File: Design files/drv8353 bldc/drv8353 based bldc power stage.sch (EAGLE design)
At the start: 110 parts, among them IC1 DRV8350RSRGZT, J3 2X6 FEMALE, J4 B06B-HCMKK

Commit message: started layout of power stage
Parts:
- removed BB2: (no value), busbar:TE3/2
- removed C1: 0.1uF, resistor:C-EUC0603K
- removed C10, C11, C12: 2200pF, rcl:C-EUC0603K
- removed C13: 1 uF, rcl:C-EUC1206K
- removed C14: .1 uF, resistor:C-EUC0805K
- removed C15, C16, C17: 1 uF, rcl:C-EUC0603K
- removed C18: .01uF, rcl:C-EUC0603K
- removed C19: 3600pF, rcl:C-EUC0603K
- removed C20: 2.2uF, rcl:C-EUC0805K
- removed C21: .047 uF, rcl:C-EUC0805K
- removed C22: 1 uF, resistor:C-EUC0603K
- removed C25: .1 uF, rcl:C-EUC0805K
- removed C26: 10 uF, rcl:C-EUC2220K
- removed C27: 1 uF, rcl:C-EUC0805K
- removed C28: .01 uF, rcl:C-EUC0603K
- removed C29: 4.7 uF, rcl:C-EUC1210K
- removed D4: DFLS1200, REV BLDC:DFLS1200
- removed IC1: DRV8350RSRGZT, REV BLDC:DRV8350RSRGZT
- removed J3: 2X6 FEMALE, pinhead:PINHD-2X6
- removed J4: B06B-HCMKK, SamacSys_Parts:B06B-HCMKK
- removed JP1: (no value), pinhead:PINHD-1X2
- removed L3: 330 uH, REV BLDC:74404084331
- removed LDO: LP2992IM5-5.0_NOPB, SamacSys_Parts:LP2992IM5-5.0_NOPB
- removed LED1: (no value), eagle-ltspice:LED_ESML0603
- removed R1, R_FB1: 10k, rcl:R-US_R0603
- removed R10, R11, R12: 56, rcl:R-US_R0603
- removed R13: 107k, rcl:R-US_R0603
- removed R14: 274k, rcl:R-US_R0603
- removed R17: 2.61, rcl:R-US_R0603
- removed R2: 330, rcl:R-US_R0603
- removed R20: 1k, rcl:R-US_R0603
- removed R3: 5K, resistor:R-US_R0603
- removed R4, R5: 0, resistor:R-US_R0603
- removed R_FB2: 2.61k, rcl:R-US_R0603
- removed S1: RDT1034, switch:RDT1034
- removed SV1: (no value), pinhead:PINHD-1X3
- removed TP10, TP11, TP12, TP15, TP19, TP32, TP33, TP34, TP36, TP40, TP5, TP6, TP7, TP8, TP9: TPB1,27, testpad:TPB1,27
- removed TVS_DIODE: TPD4S010DQAR, REV BLDC:TPD4S010DQAR
- removed U$1: ZENER, REV BLDC:ZENER
- removed U$2: BOOSTER_DOCK, REV BLDC:BOOSTER_DOCK
- added U$11, U$12, U$13, U$15, U$4, U$5: ZENER_PACK, REV BLDC:ZENER_PACK
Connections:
- removed net 3V3: J4.2, JP1.2, R1.2, R2.2, R20.2, U$2.1
- removed net AGND: IC1.AGND, R4.1, TP40.TP
- removed net BST: C18.2, IC1.BST
- removed net CPH: C21.2, IC1.CPH
- removed net CPL: C21.1, IC1.CPL
- removed net CS: IC1.NSCS, J3.10, U$2.19
- removed net DRV_VM: C25.1, C26.1, IC1.VM, SV1.2, TP15.TP
- removed net ENABLE: IC1.ENABLE, R3.1, S1.B, U$2.11
- removed net FB: C19.2, IC1.FB, R_FB1.1, R_FB2.2
- removed net HALL_A: J4.3, U$2.34
- removed net HALL_B: J4.4, U$2.33
- removed net HALL_C: J4.5, U$2.32
- removed net INHA: IC1.INHA, J3.11, U$2.40
- removed net INHB: IC1.INHB, J3.7, U$2.38
- removed net INHC: IC1.INHC, J3.6, U$2.36
- removed net INLA: IC1.INLA, J3.9, U$2.39
- removed net INLB: IC1.INLB, J3.8, U$2.37
- removed net INLC: IC1.INLC, J3.4, U$2.35
- removed net ISENA: C10.1, R10.1, U$2.27
- removed net ISENB: C11.1, R11.1, U$2.28
- removed net ISENC: C12.1, R12.1, U$2.29
- removed net MISO: IC1.SDO, J3.1, R20.1, U$2.14
- removed net MOSI: IC1.SDI, J3.3, U$2.15
- removed net N$1: C15.2, IC1.DVDD
- removed net N$13: C28.2, LDO.BYPASS
- removed net N$14: C20.1, R17.1
- removed net N$16: LED1.A, R2.1
- removed net N$2: C29.2, JP1.1, LDO.VOUT
- removed net N$20: C1.1, R3.2
- removed net NFAULT: IC1.NFAULT, LED1.C, R1.1, U$2.12
- removed net PGND: R5.1, TP19.TP, U$2.2
- removed net RCL: IC1.RCL, R13.2
- removed net RT/SD: IC1.RT/SD, R14.2
- removed net SCLK: IC1.SCLK, J3.5, U$2.7
- removed net SW: C18.1, D4.LINE, IC1.SW, L3.2
- removed net VBUCK: C19.1, C20.2, C27.2, L3.1, LDO.IN, LDO.ON/!OFF, R_FB1.2, SV1.1, U$1.LINE
- removed net VCC: C17.2, IC1.VCC
- removed net VCP: C22.2, IC1.VCP
- removed net VGLS: C16.2, IC1.VGLS
- net APHASE: now also U$5.END2; no longer IC1.SHA, TP32.TP
- net BPHASE: now also U$11.END2; no longer IC1.SHB, TP6.TP
- net CPHASE: now also U$13.END2; no longer IC1.SHC, TP12.TP
- net GHA: now also U$5.END1; no longer IC1.GHA, TP36.TP
- net GHB: now also U$11.END1; no longer IC1.GHB, TP8.TP
- net GHC: now also U$13.END1; no longer IC1.GHC, TP9.TP
- net GLA: now also U$4.END1; no longer IC1.GLA, TP33.TP
- net GLB: now also U$12.END1; no longer IC1.GLB, TP7.TP
- net GLC: now also U$15.END1; no longer IC1.GLC, TP11.TP
- net GND: no longer BB2.P@1, BB2.P@2, C1.2, C10.2, C11.2, C12.2, C13.2, C14.1, C15.1, C16.1, C17.1, C25.2, C26.2, C27.1, C28.1, C29.1, D4.GND, IC1.DGND, IC1.GND_1, IC1.GND_2, J3.12, J3.2, J4.6, LDO.GND, R13.1, R17.2, R4.2, R5.2, R_FB2.1, S1.A, S1.A1, TVS_DIODE.AGND, TVS_DIODE.GND, U$1.A, U$2.20, U$2.22
- net SLA: now also U$4.END2; no longer IC1.SLA, TP34.TP
- net SLB: now also U$12.END2; no longer IC1.SLB, TP5.TP
- net SLC: now also U$15.END2; no longer IC1.SLC, TP10.TP
- net SOA: no longer R10.2
- net SOB: no longer R11.2
- net SOC: no longer R12.2
- net VDRAIN: no longer C13.1, C14.2, C22.1, IC1.VDRAIN, IC1.VIN, R14.1, SV1.3
- net VSENA: no longer TVS_DIODE.D2+, TVS_DIODE.NC2, U$2.30
- net VSENB: no longer TVS_DIODE.D1-, TVS_DIODE.NC3, U$2.25
- net VSENC: no longer TVS_DIODE.D1+, TVS_DIODE.NC4, U$2.26
- net VSENVM: no longer TVS_DIODE.D2-, TVS_DIODE.NC1, U$2.23
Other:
- note removed: "Debug Header"
- note removed: "ESD Protection"
- note removed: "PGA_OUT test points"

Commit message: large components tenetively placed
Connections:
- net GND: now also U$16.+; no longer U$16.-
- net N$15: now also U$16.-; no longer U$16.+
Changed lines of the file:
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@@
 <wire x1="71.12" y1="40.64" x2="71.12" y2="63.5" width="0.1524" layer="91"/>
 <junction x="2.54" y="40.64"/>
-<pinref part="U$16" gate="G$1" pin="-"/>
-<wire x1="71.12" y1="63.5" x2="73.66" y2="63.5" width="0.1524" layer="91"/>
 <pinref part="C24" gate="G$1" pin="2"/>
 <wire x1="10.16" y1="45.72" x2="10.16" y2="40.64" width="0.1524" layer="91"/>
@@
 <pinref part="U$19" gate="G$1" pin="-"/>
 <pinref part="SUPPLY1" gate="GND" pin="GND"/>
+<pinref part="U$16" gate="G$1" pin="+"/>
 </segment>
 </net>
@@
 <segment>
 <pinref part="F1" gate="G$1" pin="2"/>
-<pinref part="U$16" gate="G$1" pin="+"/>
 <wire x1="66.04" y1="71.12" x2="68.58" y2="71.12" width="0.1524" layer="91"/>
 <pinref part="TP16" gate="G$1" pin="TP"/>
-<wire x1="68.58" y1="71.12" x2="73.66" y2="71.12" width="0.1524" layer="91"/>
+<wire x1="68.58" y1="71.12" x2="71.12" y2="71.12" width="0.1524" layer="91"/>
 <junction x="68.58" y="71.12"/>
+<pinref part="U$16" gate="G$1" pin="-"/>
 </segment>
 </net>

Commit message: created tenetive board connection part, did some initial routing
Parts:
- removed C24: 0.047 uF, rcl:C-EUC0603K
- removed C34, C35, C36: .047uF, rcl:C-EUC0603K
- removed R18, R24, R27, R28: 383k, rcl:R-US_R0603
- removed R19, R25, R26, R29: 9.76k, rcl:R-US_R0603
- removed U$20, U$21, U$22, U$23, U$24: NVMTS1D2N08H, REV BLDC:NVMTS1D2N08H
- added U$1, U$17, U$2, U$25, U$26, U$27: IAUT300N08S5N014, SamacSys_Parts:IAUT300N08S5N014
- U$14: value NVMTS1D2N08H -> POWER_STAGE_CONNECTOR; device REV BLDC:NVMTS1D2N08H -> REV BLDC:POWER_STAGE_CONNECTOR
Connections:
- removed net VSENA: C34.1, R24.1, R25.2
- removed net VSENB: C35.1, R26.2, R27.1
- removed net VSENC: C36.1, R28.1, R29.2
- removed net VSENVM: C24.1, R18.1, R19.2
- new net N$1: U$14.VDRAIN
- new net N$10: U$14.GHB
- new net N$11: U$14.GHC
- new net N$12: U$14.CPHASE
- new net N$13: U$14.GLC
- new net N$14: U$14.SLC
- new net N$16: U$14.SOC
- new net N$17: U$14.SOB
- new net N$18: U$14.SOA
- new net N$19: U$14.CPHASE2
- new net N$2: U$14.GND
- new net N$20: U$14.BPHASE2
- new net N$21: U$14.APHASE2
- new net N$22: U$14.VDRAIN2
- new net N$23: U$14.5V
- new net N$3: U$14.GHA
- new net N$4: U$14.APHASE
- new net N$5: U$14.GLA
- new net N$6: U$14.SLA
- new net N$7: U$14.SLB
- new net N$8: U$14.GLB
- new net N$9: U$14.BPHASE
- net APHASE: now also U$1.S, U$2.D, U$5.END1; no longer R24.2, U$14.S1, U$14.S2, U$14.S3, U$20.D1, U$20.D2, U$20.D3, U$20.D4, U$20.DT, U$5.END2
- net BPHASE: now also U$11.END1, U$17.D, U$25.S; no longer R27.2, U$11.END2, U$21.D1, U$21.D2, U$21.D3, U$21.D4, U$21.DT, U$22.S1, U$22.S2, U$22.S3
- net CPHASE: now also U$13.END1, U$26.S, U$27.D; no longer R28.2, U$13.END2, U$23.S1, U$23.S2, U$23.S3, U$24.D1, U$24.D2, U$24.D3, U$24.D4, U$24.DT
- net GHA: now also U$1.G, U$5.END2; no longer U$14.G, U$5.END1
- net GHB: now also U$11.END2, U$25.G; no longer U$11.END1, U$22.G
- net GHC: now also U$13.END2, U$26.G; no longer U$13.END1, U$23.G
- net GLA: now also U$2.G, U$4.END2; no longer U$20.G, U$4.END1
- net GLB: now also U$12.END2, U$17.G; no longer U$12.END1, U$21.G
- net GLC: now also U$15.END2, U$27.G; no longer U$15.END1, U$24.G
- net GND: no longer C24.2, C34.2, C35.2, C36.2, R19.1, R25.1, R26.1, R29.1
- net SLA: now also U$2.S, U$4.END1; no longer U$20.S1, U$20.S2, U$20.S3, U$4.END2
- net SLB: now also U$12.END1, U$17.S; no longer U$12.END2, U$21.S1, U$21.S2, U$21.S3
- net SLC: now also U$15.END1, U$27.S; no longer U$15.END2, U$24.S1, U$24.S2, U$24.S3
- net VDRAIN: now also U$1.D, U$25.D, U$26.D; no longer R18.2, U$14.D1, U$14.D2, U$14.D3, U$14.D4, U$14.DT, U$22.D1, U$22.D2, U$22.D3, U$22.D4, U$22.DT, U$23.D1, U$23.D2, U$23.D3, U$23.D4, U$23.DT
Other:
- moved on the sheet: U$11, U$12, U$13, U$15, U$4, U$5

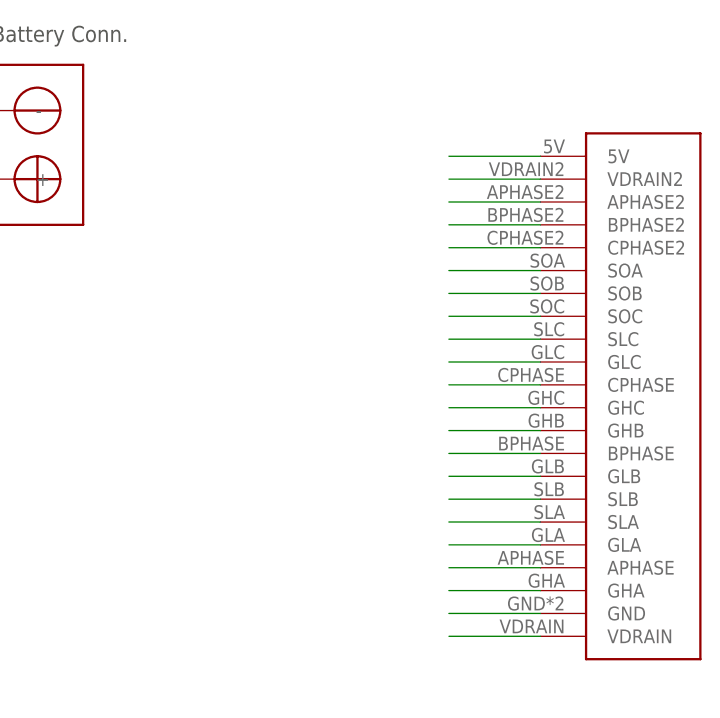
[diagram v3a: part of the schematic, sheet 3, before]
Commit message: finished most of power stage routing
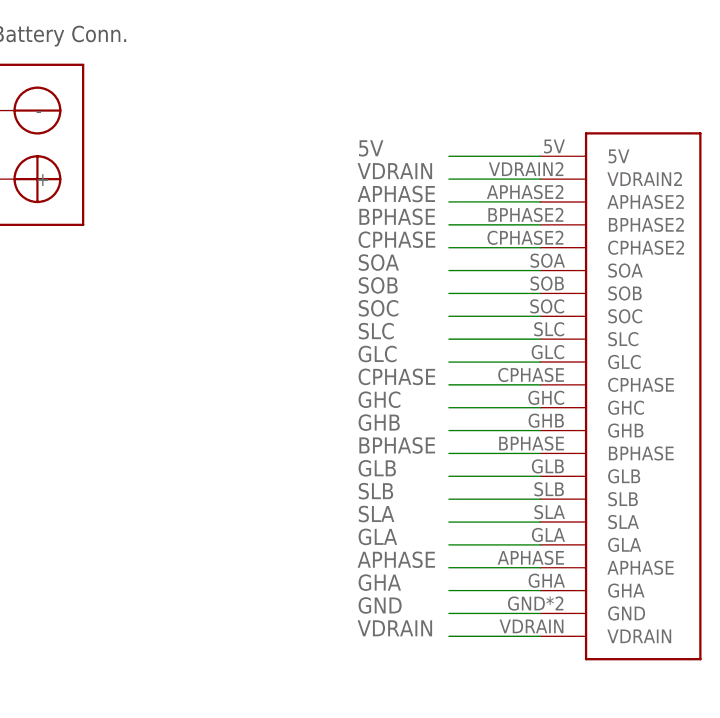
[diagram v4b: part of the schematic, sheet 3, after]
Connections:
- removed net N$1: U$14.VDRAIN
- removed net N$10: U$14.GHB
- removed net N$11: U$14.GHC
- removed net N$12: U$14.CPHASE
- removed net N$13: U$14.GLC
- removed net N$14: U$14.SLC
- removed net N$16: U$14.SOC
- removed net N$17: U$14.SOB
- removed net N$18: U$14.SOA
- removed net N$19: U$14.CPHASE2
- removed net N$2: U$14.GND
- removed net N$20: U$14.BPHASE2
- removed net N$21: U$14.APHASE2
- removed net N$22: U$14.VDRAIN2
- removed net N$23: U$14.5V
- removed net N$3: U$14.GHA
- removed net N$4: U$14.APHASE
- removed net N$5: U$14.GLA
- removed net N$6: U$14.SLA
- removed net N$7: U$14.SLB
- removed net N$8: U$14.GLB
- removed net N$9: U$14.BPHASE
- net 5V: now also U$14.5V
- net APHASE: now also U$14.APHASE, U$14.APHASE2
- net BPHASE: now also U$14.BPHASE, U$14.BPHASE2
- net CPHASE: now also U$14.CPHASE, U$14.CPHASE2
- net GHA: now also U$14.GHA
- net GHB: now also U$14.GHB
- net GHC: now also U$14.GHC
- net GLA: now also U$14.GLA
- net GLB: now also U$14.GLB
- net GLC: now also U$14.GLC
- net GND: now also U$14.GND
- net SLA: now also U$14.SLA
- net SLB: now also U$14.SLB
- net SLC: now also U$14.SLC
- net SOA: now also U$14.SOA
- net SOB: now also U$14.SOB
- net SOC: now also U$14.SOC
- net VDRAIN: now also U$14.VDRAIN, U$14.VDRAIN2
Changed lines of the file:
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@@
 <junction x="45.72" y="71.12"/>
+</segment>
+<segment>
+<pinref part="U$14" gate="G$1" pin="VDRAIN"/>
+<wire x1="137.16" y1="12.7" x2="127" y2="12.7" width="0.1524" layer="91"/>
+<label x="116.84" y="12.7" size="1.778" layer="95"/>
+</segment>
+<segment>
+<pinref part="U$14" gate="G$1" pin="VDRAIN2"/>
+<wire x1="137.16" y1="63.5" x2="127" y2="63.5" width="0.1524" layer="91"/>
+<label x="116.84" y="63.5" size="1.778" layer="95"/>
 </segment>
 </net>
@@
 <pinref part="U$16" gate="G$1" pin="+"/>
 </segment>
+<segment>
+<pinref part="U$14" gate="G$1" pin="GND"/>
+<wire x1="137.16" y1="15.24" x2="127" y2="15.24" width="0.1524" layer="91"/>
+<label x="116.84" y="15.24" size="1.778" layer="95"/>
+</segment>
 </net>
 <net name="N$15" class="0">
@@
 <pinref part="U$6" gate="G$1" pin="P$1"/>
 </segment>
+<segment>
+<pinref part="U$14" gate="G$1" pin="CPHASE"/>
+<wire x1="137.16" y1="40.64" x2="127" y2="40.64" width="0.1524" layer="91"/>
+<label x="116.84" y="40.64" size="1.778" layer="95"/>
+</segment>
+<segment>
+<pinref part="U$14" gate="G$1" pin="CPHASE2"/>
+<wire x1="137.16" y1="55.88" x2="127" y2="55.88" width="0.1524" layer="91"/>
+<label x="116.84" y="55.88" size="1.778" layer="95"/>
+</segment>
 </net>
 <net name="BPHASE" class="0">
@@
 <label x="45.72" y="10.16" size="1.778" layer="95" rot="R180" xref="yes"/>
 <pinref part="U$7" gate="G$1" pin="P$1"/>
+</segment>
+<segment>
+<pinref part="U$14" gate="G$1" pin="BPHASE"/>
+<wire x1="137.16" y1="33.02" x2="127" y2="33.02" width="0.1524" layer="91"/>
+<label x="116.84" y="33.02" size="1.778" layer="95"/>
+</segment>
+<segment>
+<pinref part="U$14" gate="G$1" pin="BPHASE2"/>
+<wire x1="137.16" y1="58.42" x2="127" y2="58.42" width="0.1524" layer="91"/>
+<label x="116.84" y="58.42" size="1.778" layer="95"/>
 </segment>
 </net>
@@
 <pinref part="U$8" gate="G$1" pin="P$1"/>
 </segment>
-</net>
-<net name="N$1" class="0">
 <segment>
-<pinref part="U$14" gate="G$1" pin="VDRAIN"/>
-<wire x1="137.16" y1="12.7" x2="127" y2="12.7" width="0.1524" layer="91"/>
+<pinref part="U$14" gate="G$1" pin="APHASE"/>
+<wire x1="137.16" y1="20.32" x2="127" y2="20.32" width="0.1524" layer="91"/>
+<label x="116.84" y="20.32" size="1.778" layer="95"/>
+</segment>
+<segment>
+<pinref part="U$14" gate="G$1" pin="APHASE2"/>
+<wire x1="137.16" y1="60.96" x2="127" y2="60.96" width="0.1524" layer="91"/>
+<label x="116.84" y="60.96" size="1.778" layer="95"/>
 </segment>
 </net>
-<net name="N$2" class="0">
-<segment>
-<pinref part="U$14" gate="G$1" pin="GND"/>
-<wire x1="137.16" y1="15.24" x2="127" y2="15.24" width="0.1524" layer="91"/>
-</segment>
-</net>
-<net name="N$3" class="0">
+<net name="GHA" class="0">
 <segment>
 <pinref part="U$14" gate="G$1" pin="GHA"/>
 <wire x1="137.16" y1="17.78" x2="127" y2="17.78" width="0.1524" layer="91"/>
+<label x="116.84" y="17.78" size="1.778" layer="95"/>
 </segment>
 </net>
-<net name="N$4" class="0">
-<segment>
-<pinref part="U$14" gate="G$1" pin="APHASE"/>
-<wire x1="137.16" y1="20.32" x2="127" y2="20.32" width="0.1524" layer="91"/>
-</segment>
-</net>
-<net name="N$5" class="0">
+<net name="GLA" class="0">
 <segment>
 <pinref part="U$14" gate="G$1" pin="GLA"/>
 <wire x1="137.16" y1="22.86" x2="127" y2="22.86" width="0.1524" layer="91"/>
+<label x="116.84" y="22.86" size="1.778" layer="95"/>
 </segment>
 </net>
-<net name="N$6" class="0">
+<net name="SLA" class="0">
 <segment>
 <pinref part="U$14" gate="G$1" pin="SLA"/>
 <wire x1="137.16" y1="25.4" x2="127" y2="25.4" width="0.1524" layer="91"/>
+<label x="116.84" y="25.4" size="1.778" layer="95"/>
 </segment>
 </net>
-<net name="N$7" class="0">
+<net name="SLB" class="0">
 <segment>
 <pinref part="U$14" gate="G$1" pin="SLB"/>
 <wire x1="137.16" y1="27.94" x2="127" y2="27.94" width="0.1524" layer="91"/>
+<label x="116.84" y="27.94" size="1.778" layer="95"/>
 </segment>
 </net>
-<net name="N$8" class="0">
+<net name="GLB" class="0">
 <segment>
 <pinref part="U$14" gate="G$1" pin="GLB"/>
 <wire x1="137.16" y1="30.48" x2="127" y2="30.48" width="0.1524" layer="91"/>
+<label x="116.84" y="30.48" size="1.778" layer="95"/>
 </segment>
 </net>
-<net name="N$9" class="0">
-<segment>
-<pinref part="U$14" gate="G$1" pin="BPHASE"/>
-<wire x1="137.16" y1="33.02" x2="127" y2="33.02" width="0.1524" layer="91"/>
-</segment>
-</net>
-<net name="N$10" class="0">
+<net name="GHB" class="0">
 <segment>
 <pinref part="U$14" gate="G$1" pin="GHB"/>
 <wire x1="137.16" y1="35.56" x2="127" y2="35.56" width="0.1524" layer="91"/>
+<label x="116.84" y="35.56" size="1.778" layer="95"/>
 </segment>
 </net>
-<net name="N$11" class="0">
+<net name="GHC" class="0">
 <segment>
 <pinref part="U$14" gate="G$1" pin="GHC"/>
 <wire x1="137.16" y1="38.1" x2="127" y2="38.1" width="0.1524" layer="91"/>
+<label x="116.84" y="38.1" size="1.778" layer="95"/>
 </segment>
 </net>
-<net name="N$12" class="0">
-<segment>
-<pinref part="U$14" gate="G$1" pin="CPHASE"/>
-<wire x1="137.16" y1="40.64" x2="127" y2="40.64" width="0.1524" layer="91"/>
-</segment>
-</net>
-<net name="N$13" class="0">
+<net name="GLC" class="0">
 <segment>
 <pinref part="U$14" gate="G$1" pin="GLC"/>
 <wire x1="137.16" y1="43.18" x2="127" y2="43.18" width="0.1524" layer="91"/>
+<label x="116.84" y="43.18" size="1.778" layer="95"/>
 </segment>
 </net>
-<net name="N$14" class="0">
+<net name="SLC" class="0">
 <segment>
 <pinref part="U$14" gate="G$1" pin="SLC"/>
 <wire x1="137.16" y1="45.72" x2="127" y2="45.72" width="0.1524" layer="91"/>
+<label x="116.84" y="45.72" size="1.778" layer="95"/>
 </segment>
 </net>
-<net name="N$16" class="0">
+<net name="SOC" class="0">
 <segment>
 <pinref part="U$14" gate="G$1" pin="SOC"/>
 <wire x1="137.16" y1="48.26" x2="127" y2="48.26" width="0.1524" layer="91"/>
+<label x="116.84" y="48.26" size="1.778" layer="95"/>
 </segment>
 </net>
-<net name="N$17" class="0">
+<net name="SOB" class="0">
 <segment>
 <pinref part="U$14" gate="G$1" pin="SOB"/>
 <wire x1="137.16" y1="50.8" x2="127" y2="50.8" width="0.1524" layer="91"/>
+<label x="116.84" y="50.8" size="1.778" layer="95"/>
 </segment>
 </net>
-<net name="N$18" class="0">
+<net name="SOA" class="0">
 <segment>
 <pinref part="U$14" gate="G$1" pin="SOA"/>
 <wire x1="137.16" y1="53.34" x2="127" y2="53.34" width="0.1524" layer="91"/>
+<label x="116.84" y="53.34" size="1.778" layer="95"/>
 </segment>
 </net>
-<net name="N$19" class="0">
-<segment>
-<pinref part="U$14" gate="G$1" pin="CPHASE2"/>
-<wire x1="137.16" y1="55.88" x2="127" y2="55.88" width="0.1524" layer="91"/>
-</segment>
-</net>
-<net name="N$20" class="0">
-<segment>
-<pinref part="U$14" gate="G$1" pin="BPHASE2"/>
-<wire x1="137.16" y1="58.42" x2="127" y2="58.42" width="0.1524" layer="91"/>
-</segment>
-</net>
-<net name="N$21" class="0">
-<segment>
-<pinref part="U$14" gate="G$1" pin="APHASE2"/>
-<wire x1="137.16" y1="60.96" x2="127" y2="60.96" width="0.1524" layer="91"/>
-</segment>
-</net>
-<net name="N$22" class="0">
-<segment>
-<pinref part="U$14" gate="G$1" pin="VDRAIN2"/>
-<wire x1="137.16" y1="63.5" x2="127" y2="63.5" width="0.1524" layer="91"/>
-</segment>
-</net>
-<net name="N$23" class="0">
+<net name="5V" class="0">
 <segment>
 <pinref part="U$14" gate="G$1" pin="5V"/>
 <wire x1="137.16" y1="66.04" x2="127" y2="66.04" width="0.1524" layer="91"/>
+<label x="116.84" y="66.04" size="1.778" layer="95"/>
 </segment>
 </net>
